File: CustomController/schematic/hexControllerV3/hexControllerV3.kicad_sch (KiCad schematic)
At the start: 49 parts, among them IC1 ESP32-S2-MINI-1-N4R2, IC2 IP5306, J1 USB_C_Receptacle_USB2.0_16P, J2 Battery, J3 Switch1, J4 Switch2, J5 Switch3, J6 Switch4, J7 Battery, J8 Conn_01x06, SW1 RotaryEncoder_Switch, SW2 SW_DIP_x01, SW3 SW_DIP_x01, SW4 SW_DIP_x01, SW5 SW_DIP_x01, SW6 SW_DIP_x01, U2 AMS1117-3.3

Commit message: Editted schematic
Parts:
- added C15, C16, C7: 100nF, Capacitor_SMD:C_0805_2012Metric_Pad1.18x1.45mm_HandSolder, symbol SamacSys_Parts:CC0805KRX7R9BB104
- added R10, R9: 4.7K, Resistor_SMD:R_0805_2012Metric, symbol Device:R
- added U3: INA260, Package_SO:TSSOP-16_4.4x5mm_P0.65mm, symbol Sensor:INA260
- added U4: BMI330, BMI330, symbol SamacSys_Parts:BMI330
- J8: footprint Connector_PinHeader_2.54mm:PinHeader_1x05_P2.54mm_Vertical -> Connector_PinHeader_2.54mm:PinHeader_2x04_P2.54mm_Vertical; symbol Connector_Generic:Conn_01x05 -> Connector_Generic:Conn_01x08
- S1, S2: value TS-1088-AR02016 -> KMR731NG; footprint TS1088AR02016 -> Button_Switch_SMD:SW_Push_1P1T_NO_CK_KMR2
- SW2, SW3, SW4, SW5, SW6: symbol Switch:SW_Push -> Switch:SW_MEC_5E
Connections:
- net +3V3: now also J8.2 (Pin_2), C15.2, C16.2, C7.1, R10.2, R9.1, U3.10 (VS), U4.12 (CSB), U4.5 (VDDIO), U4.8 (VDD); no longer U1.7 (VCC)
- net +5V: now also J8.1 (Pin_1), U1.7 (VCC)
- net GND: now also J8.8 (Pin_8), SW2.3 (K), SW2.4 (A), SW3.3 (K), SW3.4 (A), SW4.3 (K), SW4.4 (A), SW5.3 (K), SW5.4 (A), SW6.3 (K), SW6.4 (A), C15.1, C16.1, C7.2, U3.11 (GND), U3.4 (A1), U3.5 (A0), U3.6 (GND), U4.1 (SDO), U4.6 (GNDIO), U4.7 (GND); no longer SW2.2, SW3.2, SW4.2, SW5.2, SW6.2
- net INA260_OUT: now reaches C13.1, L1.2, R6.1
- net INA260_OUT: now also U3.14 (IN-), U3.15 (IN-), U3.16 (IN-); no longer J2.2 (Pin_2), J7.2 (Pin_2)
- net GPIO26: now reaches IC1.26 (IO26)
- net GPIO26: now also J8.6 (Pin_6)
- net GPIO37: now reaches IC1.33 (IO37)
- net GPIO37: now also J8.7 (Pin_7)
- net GPIO42: now reaches IC1.38 (IO42)
- net GPIO42: now also J8.5 (Pin_5)
- net TX: now reaches IC1.39 (TXD0)
- net TX: now also J8.4 (Pin_4)
- net RX: now reaches IC1.40 (RXD0)
- net RX: now also J8.3 (Pin_3)
- net Spare1 renamed SDA
- net SDA: now also R9.2, U3.8 (SDA), U4.14 (SDX); no longer J8.5 (Pin_5)
- net Spare2 renamed SCL
- net SCL: now also R10.1, U3.9 (SCL), U4.13 (SCX); no longer J8.4 (Pin_4)
- net Spare3 renamed BMI330_INT1
- net BMI330_INT1: now also U4.4 (INT1); no longer J8.3 (Pin_3)
- net Spare4 renamed BMI330_INT2
- net BMI330_INT2: now also U4.9 (INT2); no longer J8.2 (Pin_2)
- net Spare5 renamed INA260_INT
- net INA260_INT: now also U3.7 (ALERT); no longer J8.1 (Pin_1)
- new net: J2.2 (Pin_2), J7.2 (Pin_2), U3.1 (IN+), U3.12 (VBUS), U3.2 (IN+), U3.3 (IN+)
- no-connect marks 16 -> 25
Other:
- moved on the sheet: J2, J7, R8

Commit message: Updated controller schematic
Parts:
- removed C1: 22uF, CAPPM3528X210N, symbol SamacSys_Parts:TCJB226M025R0150E
- removed C10, C11, C12, C13, C14: 22uF, CAPC2012X140N, symbol SamacSys_Parts:CL21A226MAQNNNE
- removed C2: 10uF, CAPPM3216X180N, symbol SamacSys_Parts:TAJA106K016RNJ
- removed C8, C9: 10uF, Capacitor_SMD:C_0805_2012Metric, symbol Device:C
- removed IC2: IP5306, SOIC127P600X165-9N, symbol SamacSys_Parts:IP5306
- removed L1: 1uH, XAL40XX, symbol SamacSys_Parts:XAL4020-102MEC
- removed LED1, LED2, LED3, LED4, LED5: ~, KP1608SURCK, symbol SamacSys_Parts:KP-1608SURCK
- removed R7: 20R, Resistor_SMD:R_0805_2012Metric, symbol Device:R
- removed R8: 10k, Resistor_SMD:R_0805_2012Metric, symbol Device:R
- removed SW6: SW_DIP_x01, SamacSys_Parts:DTS62NV, symbol Switch:SW_MEC_5E
- removed U2: AMS1117-3.3, Package_TO_SOT_SMD:SOT-223-3_TabPin2, symbol Regulator_Linear:AMS1117-3.3
- added C1: 100nF, CAPC2012X95N, symbol SamacSys_Parts:CC0805KRX7R9BB104
- added C17, C18: 10uF, Capacitor_SMD:C_0603_1608Metric_Pad1.08x0.95mm_HandSolder, symbol Device:C
- added C19: 100nF, Capacitor_SMD:C_0603_1608Metric_Pad1.08x0.95mm_HandSolder, symbol Device:C
- added C20, C21, C22: 22uF, Capacitor_SMD:C_0603_1608Metric_Pad1.08x0.95mm_HandSolder, symbol SamacSys_Parts:CL21A226MAQNNNE
- added IC3: TPS63020DSJR, TPS63020DSJR, symbol SamacSys_Parts:TPS63020DSJR
- added L2: 1.5uH, XAL40XX, symbol SamacSys_Parts:XAL4020-102MEC
- added Q1: DMG9926UDM, Package_TO_SOT_SMD:SOT-23-6, symbol Transistor_FET:DMG9926UDM
- added R11: 1M, Resistor_SMD:R_0603_1608Metric, symbol Device:R
- added R12: 180K, Resistor_SMD:R_0603_1608Metric, symbol Device:R
- added U2: DW01A, Package_TO_SOT_SMD:SOT-23-6, symbol Battery_Management:DW01A
- R5: value 2R -> 1k
- R6: value 0.5R -> 100R
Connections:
- net +3V3: now also C20.1, C21.1, C22.1, IC3.4 (VOUT_1), IC3.5 (VOUT_2), R11.1
- net +5V: now also C17.1, C18.1, IC3.10 (VIN_1), IC3.11 (VIN_2)
- net +5V USB: no longer R5.1
- net GND: now also R5.1, C17.2, C18.2, C19.2, C20.2, C21.2, C22.2, IC3.15 (PGND_1), IC3.16 (PGND_2), IC3.17 (PGND_3), IC3.18 (PGND_4), IC3.19 (PGND_5), IC3.2 (GND), IC3.20 (PGND_6), IC3.21 (PGND_7), IC3.22 (PGND_8), IC3.23 (PGND_9), Q1.1 (D1), R12.2; no longer J2.1 (Pin_1), J7.1 (Pin_1)
- net INA260_OUT: no longer R6.1
- net BAT+: now reaches J2.2 (Pin_2), J7.2 (Pin_2), U3.1 (IN+), U3.12 (VBUS), U3.2 (IN+), U3.3 (IN+)
- net BAT+: now also R6.2
- net at R5.2: now also U2.2 (CS)
- new net: C1.1, J2.1 (Pin_1), J7.1 (Pin_1), Q1.3 (S2), U2.6 (GND)
- new net: C1.2, R6.1, U2.5 (VCC)
- new net: Q1.2 (S1/D2), Q1.5 (S1/D2)
- new net: Q1.4 (G2), U2.1 (OD)
- new net: Q1.6 (G1), U2.3 (OC)
- new net: IC3.3 (FB), R11.2, R12.1
- new net: C19.1, IC3.1 (VINA), IC3.12 (EN), IC3.13 (PS/SYNC)
- new net: IC3.6 (L2_1), IC3.7 (L2_2), L2.2
- new net: IC3.8 (L1_1), IC3.9 (L1_2), L2.1
- no-connect marks 25 -> 26
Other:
- note added: "Current Sensor"
- note added: "ESP32"
- note added: "IMU"
- note added: "Input"
- note added: "Voltage Reg"
- moved on the sheet: C15, C16, C3, C4, C5, C6, C7, IC1, J1, J2, J3, J4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

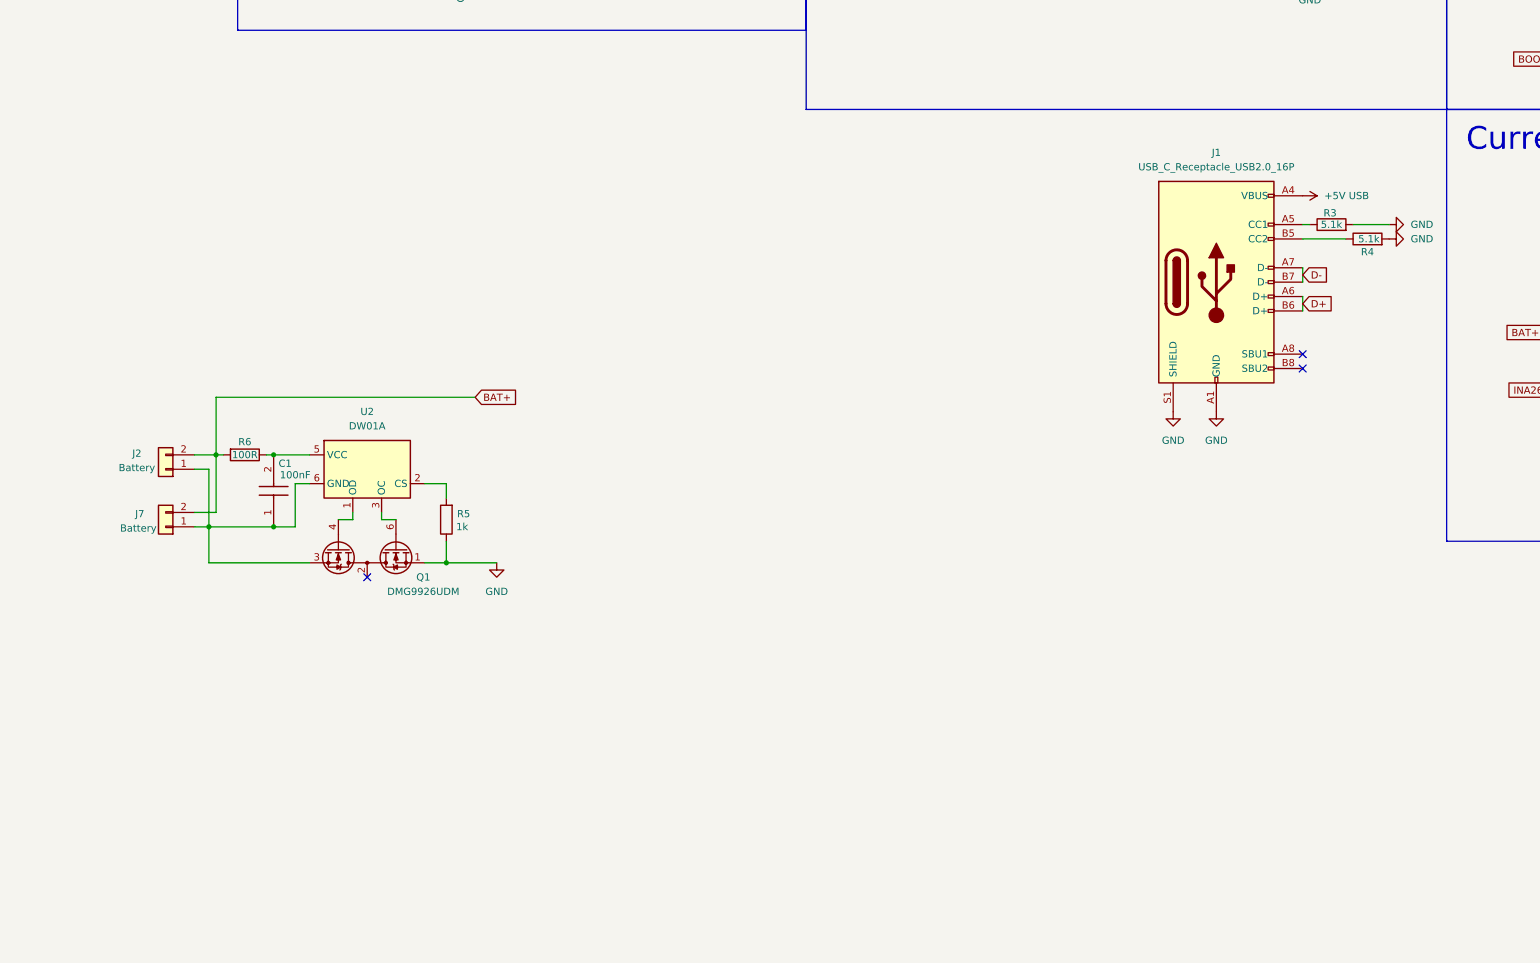
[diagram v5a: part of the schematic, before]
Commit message: Changed schematic
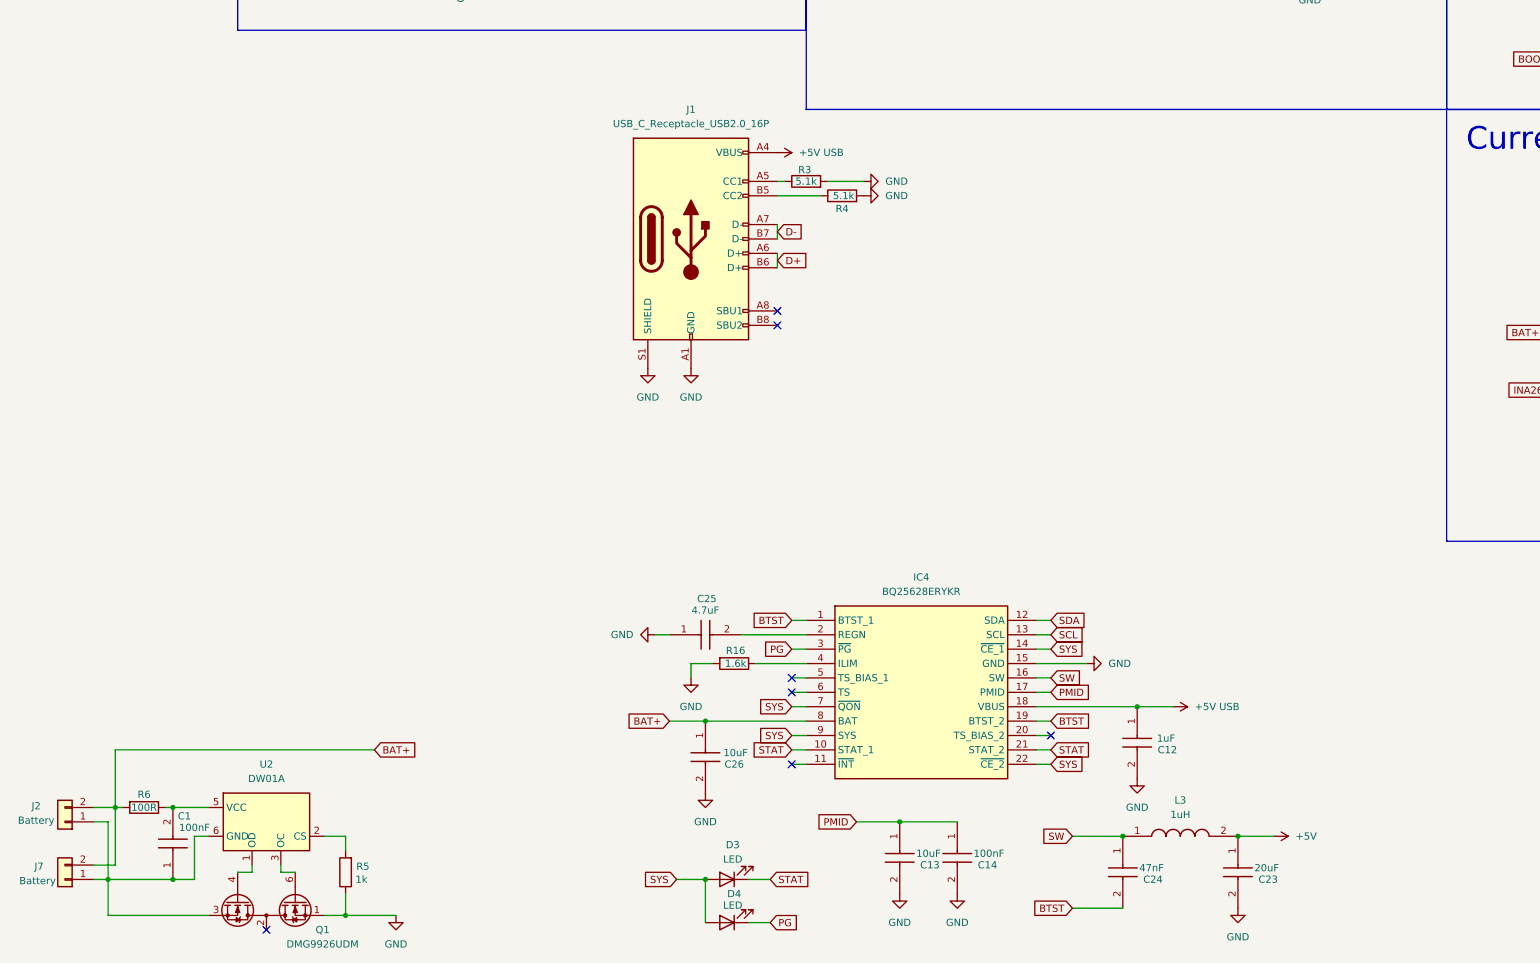
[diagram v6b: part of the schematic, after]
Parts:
- added C12: 1uF, Capacitor_SMD:C_0805_2012Metric, symbol SamacSys_Parts:CC0805KRX7R9BB104
- added C13, C26: 10uF, Capacitor_SMD:C_0805_2012Metric, symbol SamacSys_Parts:CC0805KRX7R9BB104
- added C14: 100nF, Capacitor_SMD:C_0805_2012Metric, symbol SamacSys_Parts:CC0805KRX7R9BB104
- added C23: 20uF, Capacitor_SMD:C_0805_2012Metric, symbol SamacSys_Parts:CC0805KRX7R9BB104
- added C24: 47nF, Capacitor_SMD:C_0805_2012Metric, symbol SamacSys_Parts:CC0805KRX7R9BB104
- added C25: 4.7uF, Capacitor_SMD:C_0805_2012Metric, symbol SamacSys_Parts:CC0805KRX7R9BB104
- added D3, D4: LED, Diode_SMD:D_0402_1005Metric, symbol Device:LED
- added IC4: BQ25628ERYKR, BQ25622ERYKR, symbol SamacSys_Parts:BQ25628ERYKR
- added L3: 1uH, XAL40XX, symbol SamacSys_Parts:XAL4020-102MEC
- added R16: 1.6k, Resistor_SMD:R_0805_2012Metric, symbol Device:R
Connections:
- net +5V: now also C23.1, L3.2
- net +5V USB: now also C12.1, IC4.18 (VBUS)
- net BAT+: now also C26.1, IC4.8 (BAT)
- net GND: now also C12.2, C13.2, C14.2, C23.2, C25.1, C26.2, IC4.15 (GND), R16.2
- net SCL: now also IC4.13 (SCL)
- net SDA: now also IC4.12 (SDA)
- new net: C25.2, IC4.2 (REGN)
- new net: IC4.4 (ILIM), R16.1
- new net BTST: C24.2, IC4.1 (BTST_1), IC4.19 (BTST_2)
- new net PG: D4.1 (K), IC4.3 (~{PG})
- new net PMID: C13.1, C14.1, IC4.17 (PMID)
- new net STAT: D3.1 (K), IC4.10 (STAT_1), IC4.21 (STAT_2)
- new net SW: C24.1, IC4.16 (SW), L3.1
- new net SYS: D3.2 (A), D4.2 (A), IC4.14 (~{CE_1}), IC4.22 (~{CE_2}), IC4.7 (~{QON}), IC4.9 (SYS)
- no-connect marks 26 -> 30
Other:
- moved on the sheet: C1, J1, J2, J7, Q1, R3, R4, R5, R6, U2
